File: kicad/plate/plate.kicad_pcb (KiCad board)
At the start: 2 copper layers, 231.6 x 92.5 mm, 52 parts, among them SW1 EC_SW, SW10 EC_SW, SW11 EC_SW, SW12 EC_SW, SW13 EC_SW, SW14 EC_SW, SW15 EC_SW, SW16 EC_SW, SW17 EC_SW, SW18 EC_SW, SW19 EC_SW, SW2 EC_SW, SW20 EC_SW, SW21 EC_SW, SW22 EC_SW, SW23 EC_SW, SW24 EC_SW, SW25 EC_SW, SW26 EC_SW, SW27 EC_SW, SW28 EC_SW, SW29 EC_SW, SW3 EC_SW, SW30 EC_SW, SW31 EC_SW, SW32 EC_SW, SW33 EC_SW, SW34 EC_SW, SW4 EC_SW, SW5 EC_SW, SW6 EC_SW, SW7 EC_SW, SW8 EC_SW, SW9 EC_SW

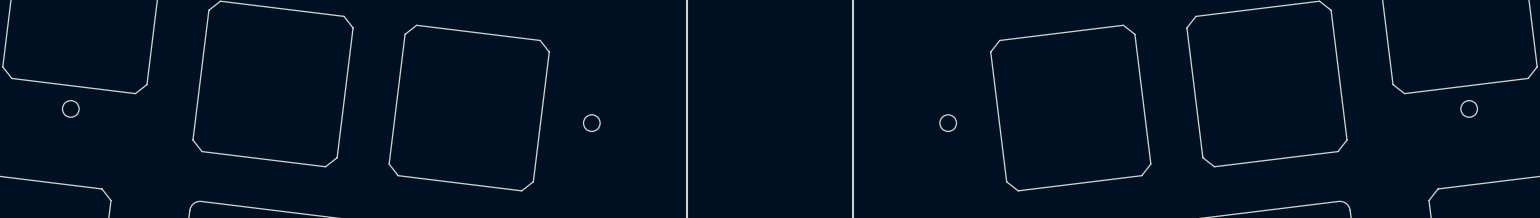
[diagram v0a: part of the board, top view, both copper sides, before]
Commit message: Clean up after prototyping
- Doc update
- remove uncessary files
- remove two more mounting holes in the "chiffre gap" area
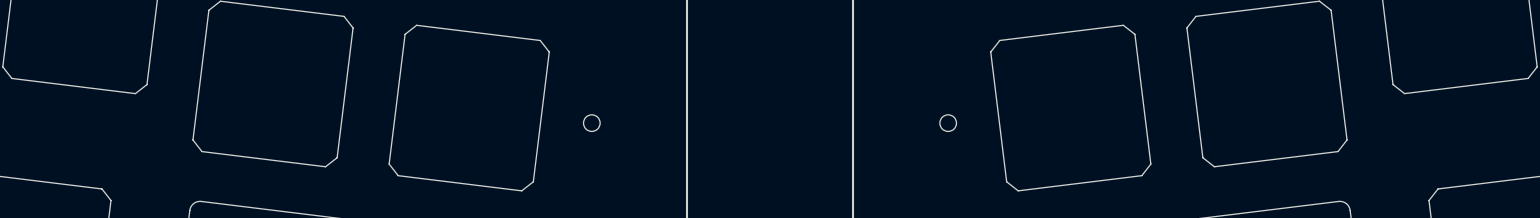
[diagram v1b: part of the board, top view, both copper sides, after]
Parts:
- removed H17, H18: M2 Hole, capacitive_sensors:MountingHole_1.6mm_M2_tapped
- moved H8 132.8 mm to (126.4, 136.8)
- moved H16 124.1 mm to (208.7, 132.1)
- moved H14 122.2 mm to (250.7, 103.0)
- moved H10 97.2 mm to (172.1, 88.6)
- moved H5 94.2 mm to (42.6, 103.0)
- moved H6 89.0 mm to (129.5, 118.4)
- moved H11 88.7 mm to (209.4, 79.2)
- moved H2 71.5 mm to (83.9, 79.2)
- moved H7 51.1 mm to (84.6, 132.1)
- moved H4 50.2 mm to (134.1, 80.6)
- moved H12 47.6 mm to (248.4, 84.1)
- moved H3 38.9 mm to (121.1, 88.6)
- moved H13 18.6 mm to (163.8, 118.4)
- moved H15 18.6 mm to (166.9, 136.8)
- moved H9 15.2 mm to (159.2, 80.6)
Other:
- board text removed: "JLCJLCJLCJLC"
